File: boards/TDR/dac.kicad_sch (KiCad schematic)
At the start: 8 parts, among them U15 MCP4822, U4 TLV3541

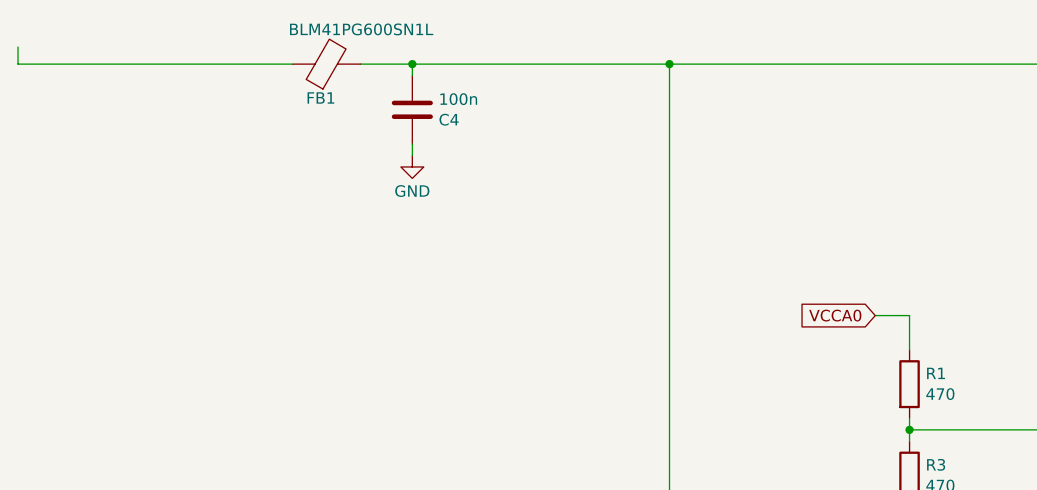
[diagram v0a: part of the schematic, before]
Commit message: change crystal footprint and roughly finish schematic
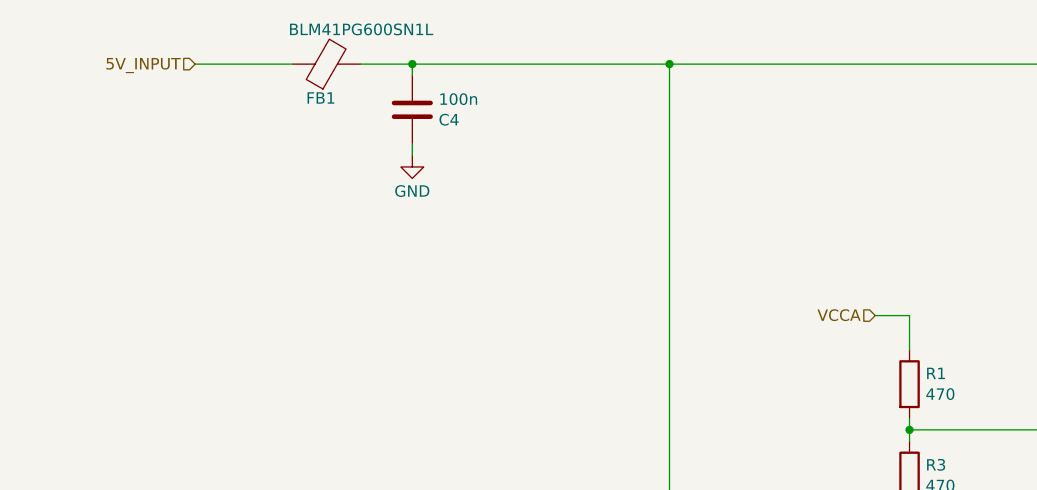
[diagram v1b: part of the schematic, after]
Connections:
- net 5V_INPUT: now reaches FB1.1
- net VCCA0 renamed VCCA
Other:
- company: (none) -> Radovan Blažek
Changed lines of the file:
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@@
-(kicad_sch (version 20200618) (host eeschema "(5.99.0-2053-g67bd49b4a)")
+(kicad_sch (version 20200618) (host eeschema "(5.99.0-2073-gbb1afb747)")
   (page 5 5)
   (paper "A4")
+  (title_block
+    (date "2020-06-30")
+    (rev "A")
+    (company "Radovan Blažek")
+    (comment 3 "In preparation")
+    (comment 4 "EN")
+  )
   (junction (at 92.075 47.625) (diameter 0) (color 0 0 0 0))
   (junction (at 120.65 47.625) (diameter 0) (color 0 0 0 0))
@@
   (junction (at 162.56 114.3) (diameter 0) (color 0 0 0 0))
   (junction (at 195.58 90.805) (diameter 0) (color 0 0 0 0))
-  (wire (pts (xy 48.26 45.72) (xy 48.26 47.625))
-    (stroke (width 0) (type solid) (color 0 0 0 0))
-  )
-  (wire (pts (xy 48.26 47.625) (xy 78.74 47.625))
+  (wire (pts (xy 67.945 47.625) (xy 78.74 47.625))
     (stroke (width 0) (type solid) (color 0 0 0 0))
   )
@@
     (stroke (width 0) (type solid) (color 0 0 0 0))
   )
-  (global_label "VCCA0" (shape input) (at 143.51 75.565 180)
+  (hierarchical_label "5V_INPUT" (shape input) (at 67.945 47.625 180)
     (effects (font (size 1.27 1.27)) (justify right))
   )
@@
     (effects (font (size 1.27 1.27)) (justify left))
   )
+  (hierarchical_label "VCCA" (shape input) (at 143.51 75.565 180)
+    (effects (font (size 1.27 1.27)) (justify right))
+  )
   (hierarchical_label "OUT_A" (shape output) (at 205.74 90.805 0)

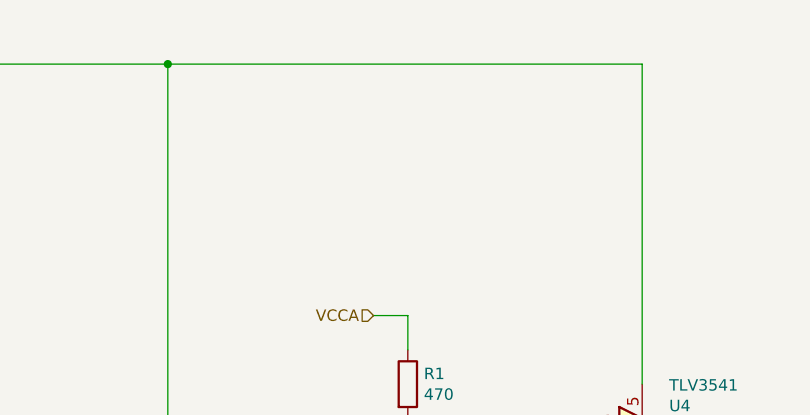
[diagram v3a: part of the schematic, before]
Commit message: route almost all nets except VCCA, VCCAUX and maybe some others
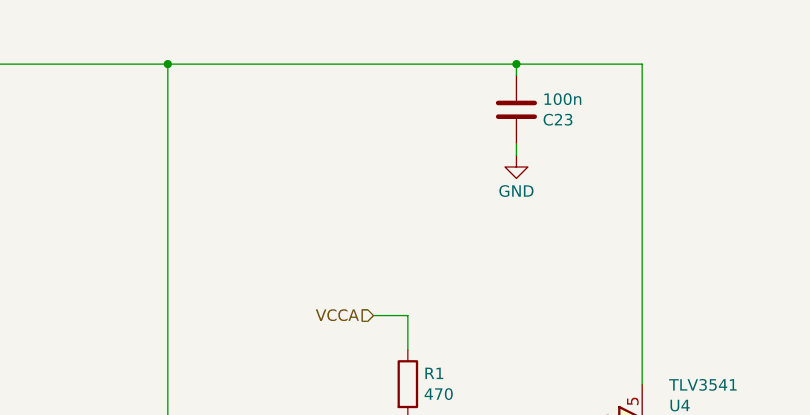
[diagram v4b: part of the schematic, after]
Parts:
- added C23: 100n, Capacitor_SMD:C_0402_1005Metric, symbol Device:C
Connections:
- net GND: now also C23.2
- net at C4.1, FB1.2, U15.1 (Vdd)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: now also C23.1
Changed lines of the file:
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@@
-(kicad_sch (version 20200618) (host eeschema "(5.99.0-2195-g476558ece)")
+(kicad_sch (version 20200618) (host eeschema "(5.99.0-2241-g37ce9fb84)")
   (page 1 5)
   (paper "A4")
@@
   (junction (at 120.65 47.625) (diameter 0) (color 0 0 0 0))
   (junction (at 147.32 88.265) (diameter 0) (color 0 0 0 0))
+  (junction (at 159.385 47.625) (diameter 0) (color 0 0 0 0))
   (junction (at 162.56 114.3) (diameter 0) (color 0 0 0 0))
   (junction (at 195.58 90.805) (diameter 0) (color 0 0 0 0))
@@
     (stroke (width 0) (type solid) (color 0 0 0 0))
   )
-  (wire (pts (xy 120.65 47.625) (xy 173.355 47.625))
+  (wire (pts (xy 120.65 47.625) (xy 159.385 47.625))
     (stroke (width 0) (type solid) (color 0 0 0 0))
   )
@@
   )
   (wire (pts (xy 155.575 114.3) (xy 162.56 114.3))
+    (stroke (width 0) (type solid) (color 0 0 0 0))
+  )
+  (wire (pts (xy 159.385 47.625) (xy 159.385 48.895))
+    (stroke (width 0) (type solid) (color 0 0 0 0))
+  )
+  (wire (pts (xy 159.385 47.625) (xy 173.355 47.625))
+    (stroke (width 0) (type solid) (color 0 0 0 0))
+  )
+  (wire (pts (xy 159.385 56.515) (xy 159.385 57.785))
     (stroke (width 0) (type solid) (color 0 0 0 0))
   )
@@
     )
     (property "Datasheet" "" (id 3) (at 147.32 98.425 0)
+      (effects (font (size 1.27 1.27)) hide)
+    )
+  )
+  (symbol (lib_id "power:GND") (at 159.385 57.785 0) (unit 1)
+    (in_bom yes) (on_board yes)
+    (property "Reference" "#PWR0145" (id 0) (at 159.385 64.135 0)
+      (effects (font (size 1.27 1.27)) hide)
+    )
+    (property "Value" "GND" (id 1) (at 159.385 61.7728 0))
+    (property "Footprint" "" (id 2) (at 159.385 57.785 0)
+      (effects (font (size 1.27 1.27)) hide)
+    )
+    (property "Datasheet" "" (id 3) (at 159.385 57.785 0)
       (effects (font (size 1.27 1.27)) hide)
     )
@@
       (effects (font (size 1.27 1.27)) hide)
     )
+  )
+  (symbol (lib_id "Device:C") (at 159.385 52.705 0) (unit 1)
+    (in_bom yes) (on_board yes)
+    (property "Reference" "C23" (id 0) (at 162.306 53.848 0)
+      (effects (font (size 1.27 1.27)) (justify left))
+    )
+    (property "Value" "100n" (id 1) (at 162.306 51.562 0)
+      (effects (font (size 1.27 1.27)) (justify left))
+    )
+    (property "Footprint" "Capacitor_SMD:C_0402_1005Metric" (id 2) (at 160.3502 56.515 0)
+      (effects (font (size 1.27 1.27)) hide)
+    )
+    (property "Datasheet" "~" (id 3) (at 159.385 52.705 0)
+      (effects (font (size 1.27 1.27)) hide)
+    )

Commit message: hopefully PCB is done
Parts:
- added C27, C29: 1u, Capacitor_SMD:C_0805_2012Metric, symbol Device:C
- added C31: 100n, Capacitor_SMD:C_0402_1005Metric, symbol Device:C
- added U16: MIC5504-3.3YM5, Package_TO_SOT_SMD:SOT-23-5, symbol Regulator_Linear:MIC5504-3.3YM5
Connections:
- net 5V_INPUT: now also C27.1, U16.1 (VIN), U16.3 (EN); no longer FB1.1
- net GND: now also C27.2, C29.2, C31.1, U16.2 (GND)
- net at R1.2, R3.1, U4.1 (+): now also C31.2
- net at C23.1, FB1.2, U4.5 (V+): no longer C4.1, U15.1 (Vdd)
- new net: C29.1, C4.1, FB1.1, U15.1 (Vdd), U16.5 (VOUT)
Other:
- moved on the sheet: C23, C4, FB1, R1, R3, R8, R9, U15, U4

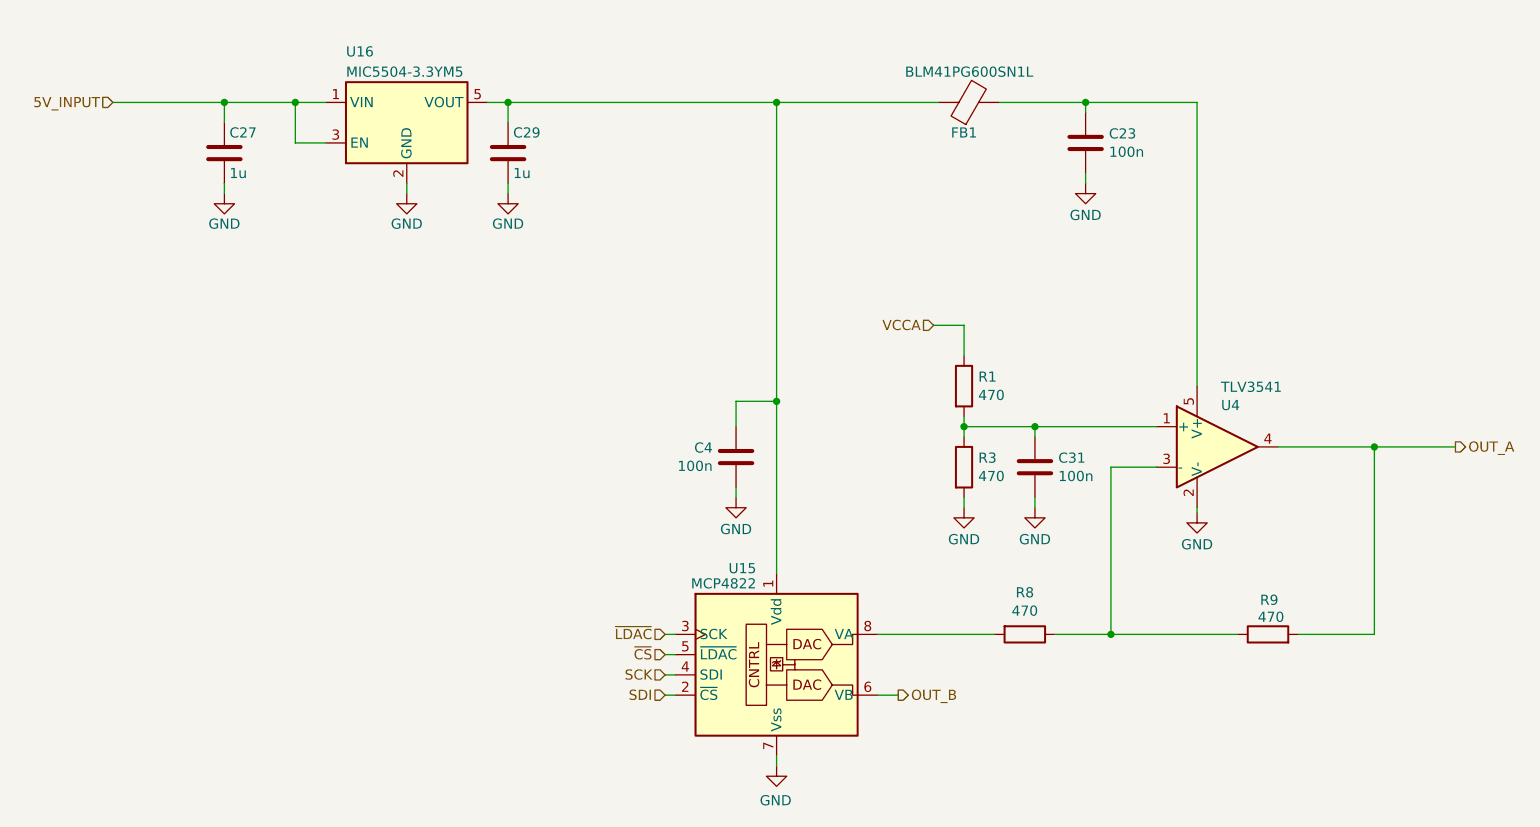
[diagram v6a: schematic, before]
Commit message: Add LD39050PUR feedback resistor values, fixed regulator enable
Fixes #1
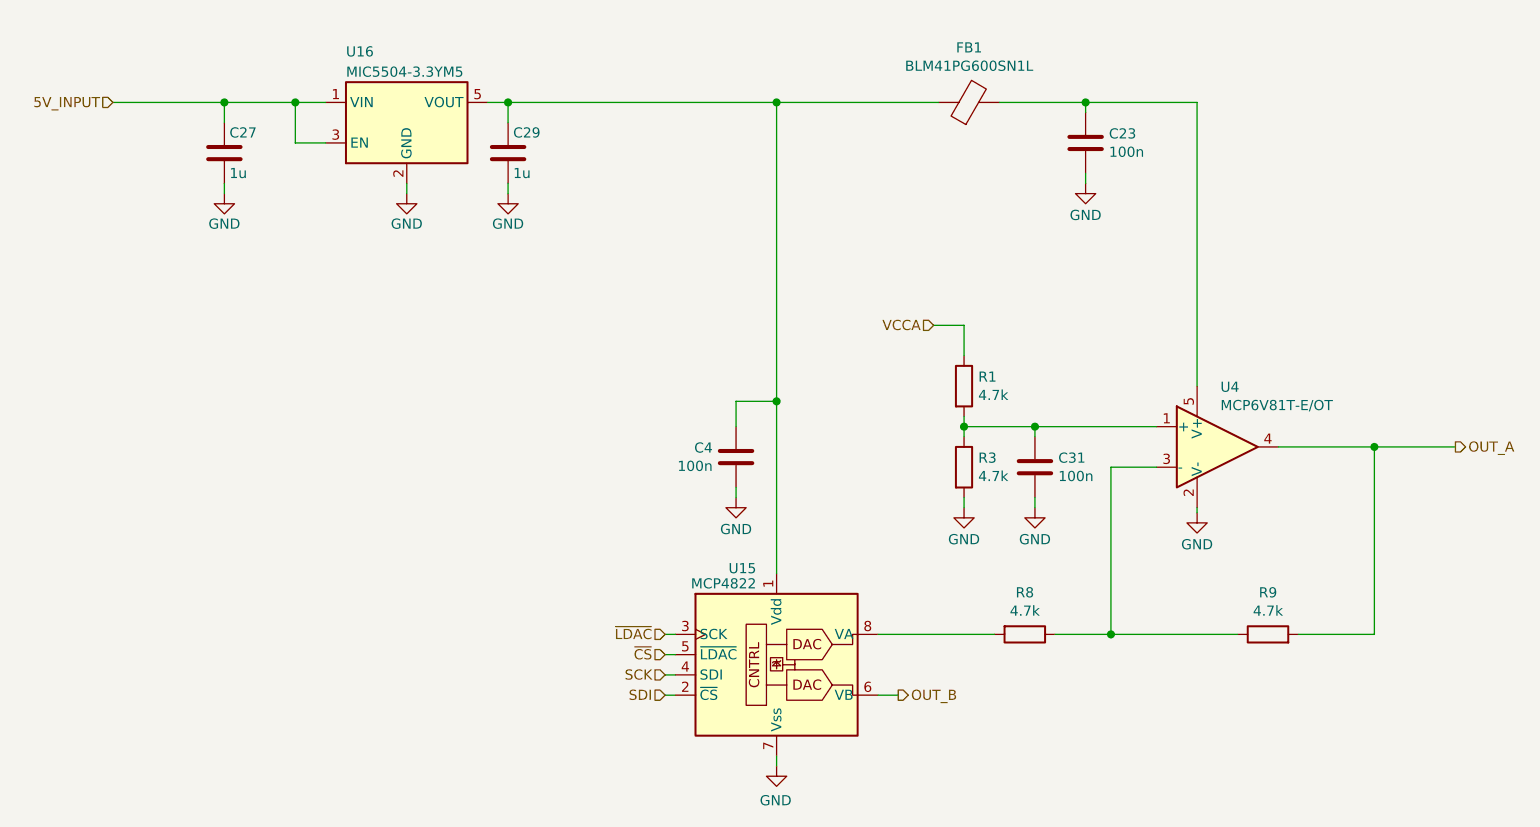
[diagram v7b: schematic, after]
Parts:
- R1, R3, R8, R9: value 470 -> 4.7k
- U4: value TLV3541 -> MCP6V81T-E/OT
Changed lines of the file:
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@@
-(kicad_sch (version 20200618) (host eeschema "(5.99.0-2250-gafd432e68)")
-  (page 5 5)
+(kicad_sch (version 20200714) (host eeschema "(5.99.0-2491-g71882a7b0)")
+  (page 1 5)
   (paper "A4")
   (title_block
@@
     (comment 4 "EN")
   )
-  (junction (at 74.295 53.34) (diameter 0) (color 0 0 0 0))
-  (junction (at 83.185 53.34) (diameter 0) (color 0 0 0 0))
-  (junction (at 109.855 53.34) (diameter 0) (color 0 0 0 0))
-  (junction (at 143.51 53.34) (diameter 0) (color 0 0 0 0))
-  (junction (at 143.51 90.805) (diameter 0) (color 0 0 0 0))
-  (junction (at 167.005 93.98) (diameter 0) (color 0 0 0 0))
-  (junction (at 175.895 93.98) (diameter 0) (color 0 0 0 0))
-  (junction (at 182.245 53.34) (diameter 0) (color 0 0 0 0))
-  (junction (at 185.42 120.015) (diameter 0) (color 0 0 0 0))
-  (junction (at 218.44 96.52) (diameter 0) (color 0 0 0 0))
+  (junction (at 74.295 53.34) (diameter 1.016) (color 0 0 0 0))
+  (junction (at 83.185 53.34) (diameter 1.016) (color 0 0 0 0))
+  (junction (at 109.855 53.34) (diameter 1.016) (color 0 0 0 0))
+  (junction (at 143.51 53.34) (diameter 1.016) (color 0 0 0 0))
+  (junction (at 143.51 90.805) (diameter 1.016) (color 0 0 0 0))
+  (junction (at 167.005 93.98) (diameter 1.016) (color 0 0 0 0))
+  (junction (at 175.895 93.98) (diameter 1.016) (color 0 0 0 0))
+  (junction (at 182.245 53.34) (diameter 1.016) (color 0 0 0 0))
+  (junction (at 185.42 120.015) (diameter 1.016) (color 0 0 0 0))
+  (junction (at 218.44 96.52) (diameter 1.016) (color 0 0 0 0))
   (wire (pts (xy 60.325 53.34) (xy 74.295 53.34))
     (stroke (width 0) (type solid) (color 0 0 0 0))
@@
       (effects (font (size 1.27 1.27)) (justify left))
     )
-    (property "Value" "470" (id 1) (at 168.7831 90.0493 0)
+    (property "Value" "4.7k" (id 1) (at 168.783 90.049 0)
       (effects (font (size 1.27 1.27)) (justify left))
     )
@@
       (effects (font (size 1.27 1.27)) (justify left))
     )
-    (property "Value" "470" (id 1) (at 168.7831 100.2093 0)
+    (property "Value" "4.7k" (id 1) (at 168.783 100.209 0)
       (effects (font (size 1.27 1.27)) (justify left))
     )
@@
     (in_bom yes) (on_board yes)
     (property "Reference" "R8" (id 0) (at 174.625 114.7888 90))
-    (property "Value" "470" (id 1) (at 174.625 117.087 90))
+    (property "Value" "4.7k" (id 1) (at 174.625 117.0875 90))
     (property "Footprint" "Resistor_SMD:R_0805_2012Metric" (id 2) (at 174.625 118.237 90)
       (effects (font (size 1.27 1.27)) hide)
@@
   (symbol (lib_id "Device:R") (at 205.105 120.015 90) (unit 1)
     (in_bom yes) (on_board yes)
-    (property "Reference" "R9" (id 0) (at 205.2574 115.7224 90))
-    (property "Value" "470" (id 1) (at 205.486 117.856 90))
+    (property "Reference" "R9" (id 0) (at 205.105 114.7888 90))
+    (property "Value" "4.7k" (id 1) (at 205.105 117.0875 90))
     (property "Footprint" "Resistor_SMD:R_0805_2012Metric" (id 2) (at 205.105 121.793 90)
       (effects (font (size 1.27 1.27)) hide)
@@
   (symbol (lib_id "Device:Ferrite_Bead") (at 167.64 53.34 90) (unit 1)
     (in_bom yes) (on_board yes)
-    (property "Reference" "FB1" (id 0) (at 167.005 57.15 90))
-    (property "Value" "BLM41PG600SN1L" (id 1) (at 167.64 49.53 90))
+    (property "Reference" "FB1" (id 0) (at 167.64 46.4882 90))
+    (property "Value" "BLM41PG600SN1L" (id 1) (at 167.64 48.7869 90))
     (property "Footprint" "Inductor_SMD:L_1806_4516Metric" (id 2) (at 167.64 55.118 90)
       (effects (font (size 1.27 1.27)) hide)
@@
   (symbol (lib_id "Amplifier_Operational:LMV321") (at 198.755 96.52 0) (unit 1)
     (in_bom yes) (on_board yes)
-    (property "Reference" "U4" (id 0) (at 199.2122 91.313 0)
-      (effects (font (size 1.27 1.27)) (justify left))
-    )
-    (property "Value" "TLV3541" (id 1) (at 199.2122 89.027 0)
-      (effects (font (size 1.27 1.27)) (justify left))
-    )
+    (property "Reference" "U4" (id 0) (at 199.1361 89.0206 0)
+      (effects (font (size 1.27 1.27)) (justify left))
+    )
+    (property "Value" "MCP6V81T-E/OT" (id 1) (at 199.1361 91.3193 0)
+      (effects (font (size 1.27 1.27)) (justify left))
+    )
